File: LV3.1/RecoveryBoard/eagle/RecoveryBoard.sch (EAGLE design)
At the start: 92 parts, among them IC1 BD62120AEFJ-E2, Q1 BSS123, Q2 BSS123, Q3 BSS123, Q6 MOSFET-PCH-SOT23-6, U1 STM32F042K6, U10 TPS63070, Y1 ECS-160-10-36Q-ES-TR

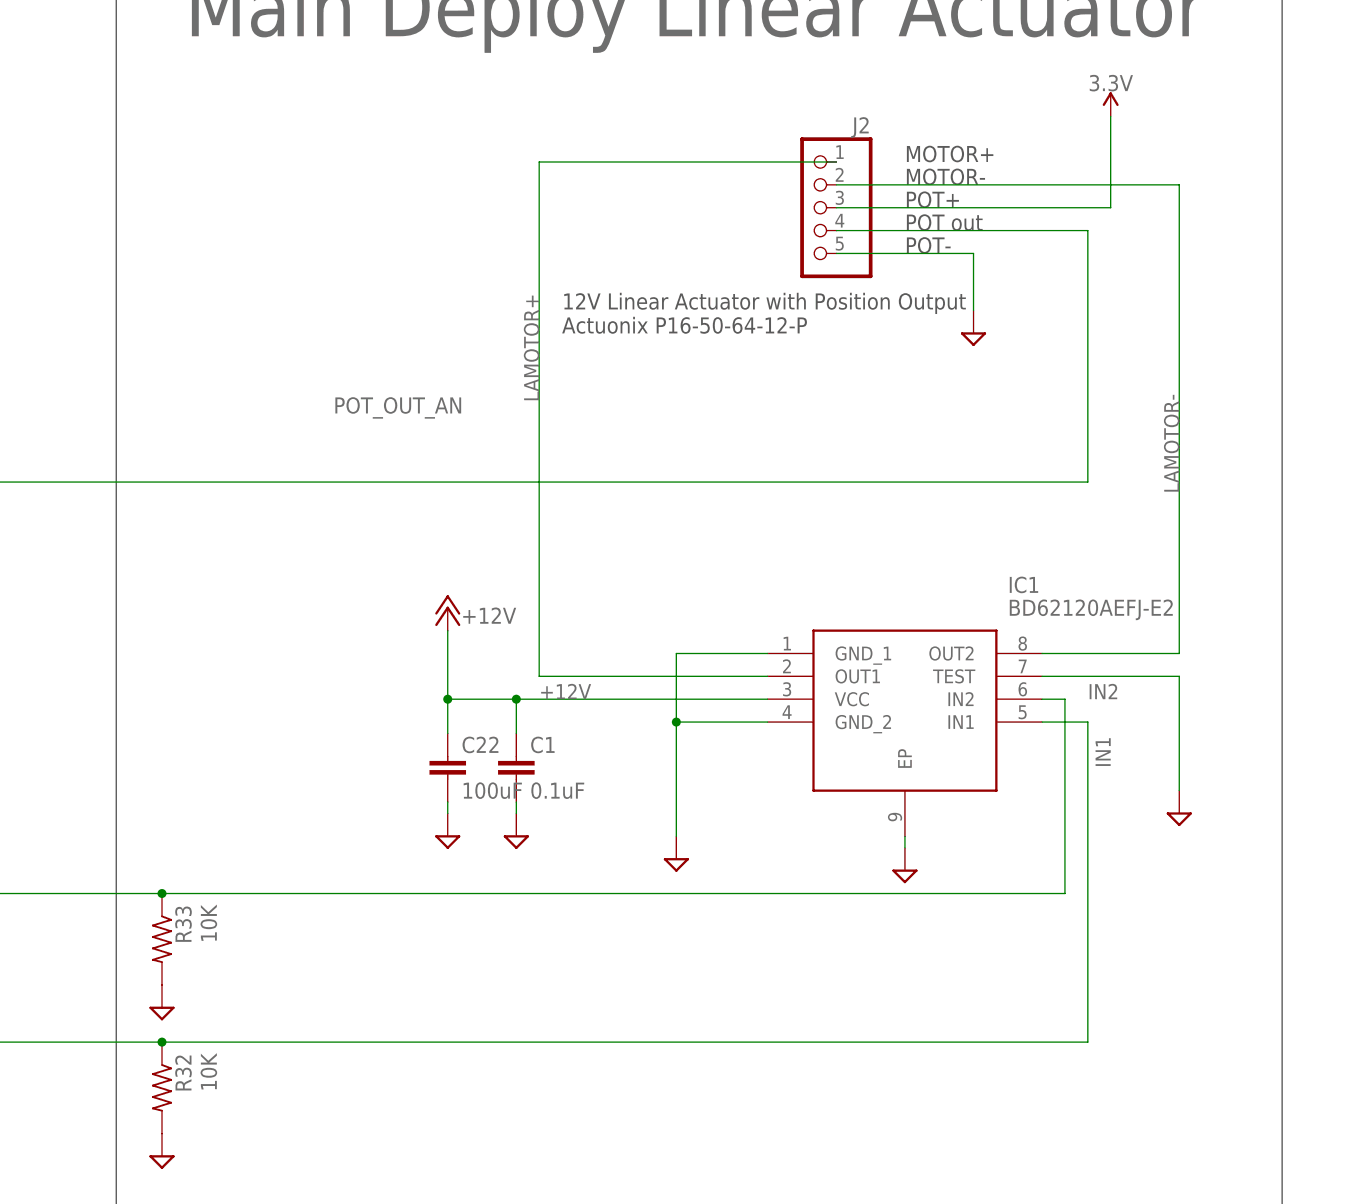
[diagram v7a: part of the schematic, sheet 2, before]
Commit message: adding new hbridge schematic
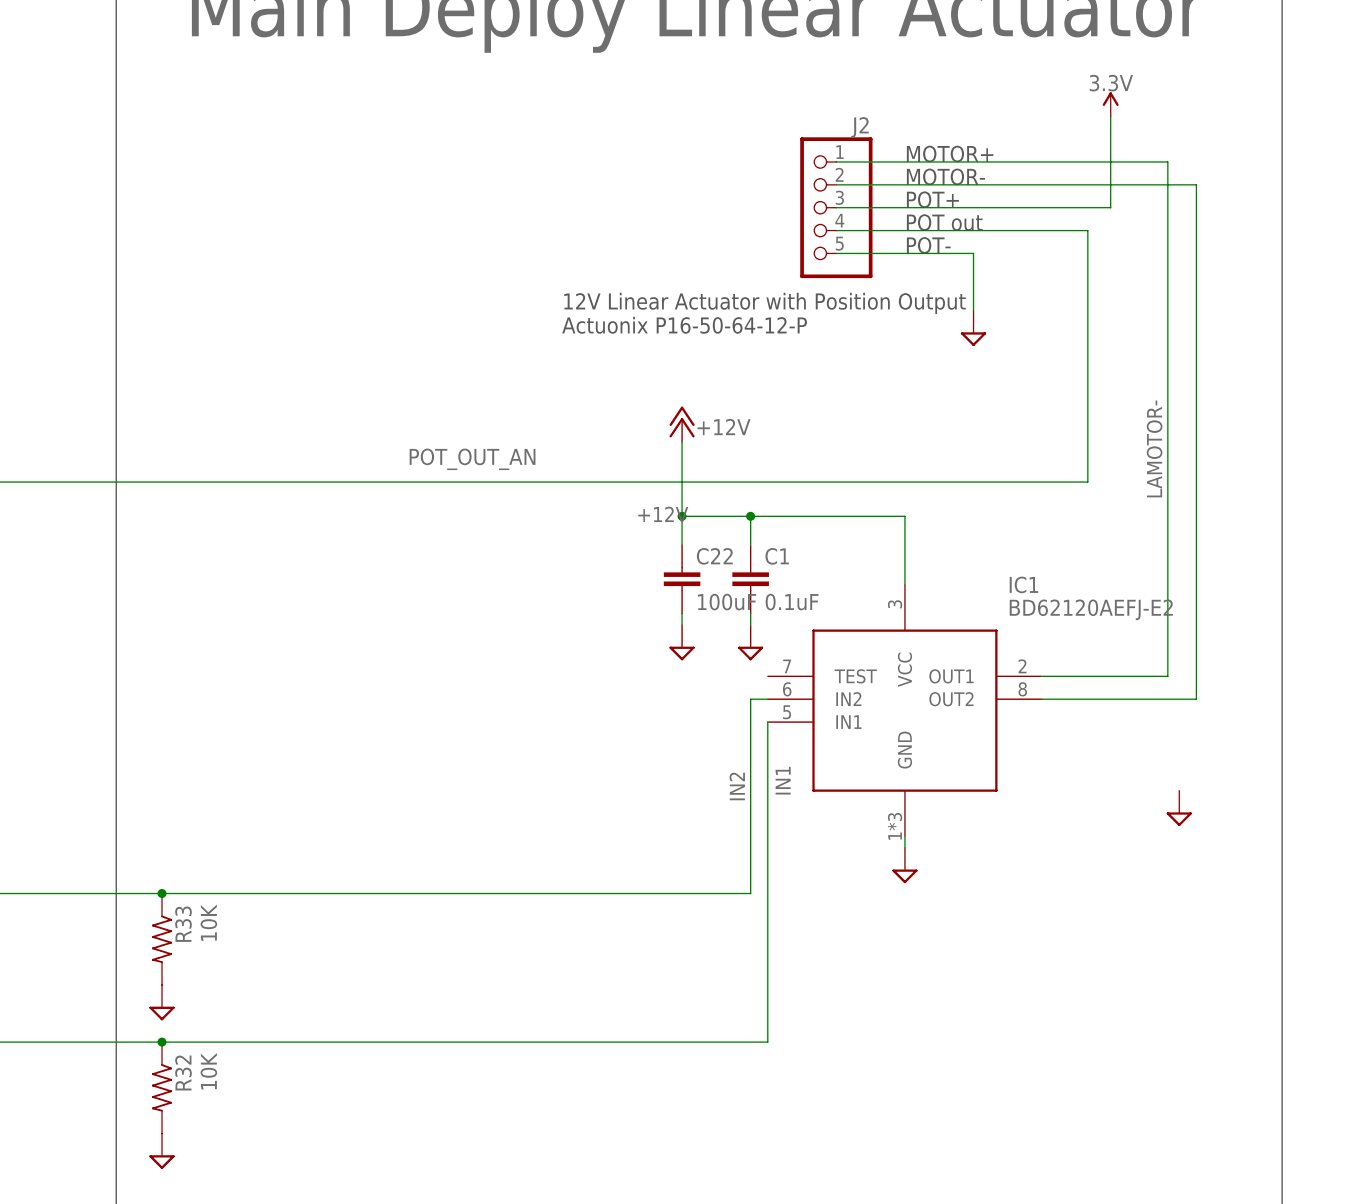
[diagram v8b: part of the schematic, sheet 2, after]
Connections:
- removed net LAMOTOR+: IC1.OUT1, J2.1
- new net N$8: IC1.OUT2, J2.2
- net GND: now also IC1.GND; no longer IC1.EP, IC1.GND_1, IC1.GND_2, IC1.TEST
- net LAMOTOR-: now also IC1.OUT1, J2.1; no longer IC1.OUT2, J2.2
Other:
- moved on the sheet: C1, C22
